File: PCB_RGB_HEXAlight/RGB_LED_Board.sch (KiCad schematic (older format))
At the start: 14 parts, among them P1 CONN_5, U1 RED DRIVER, U2 GREEN DRIVER, U3 BLUEDRIVER

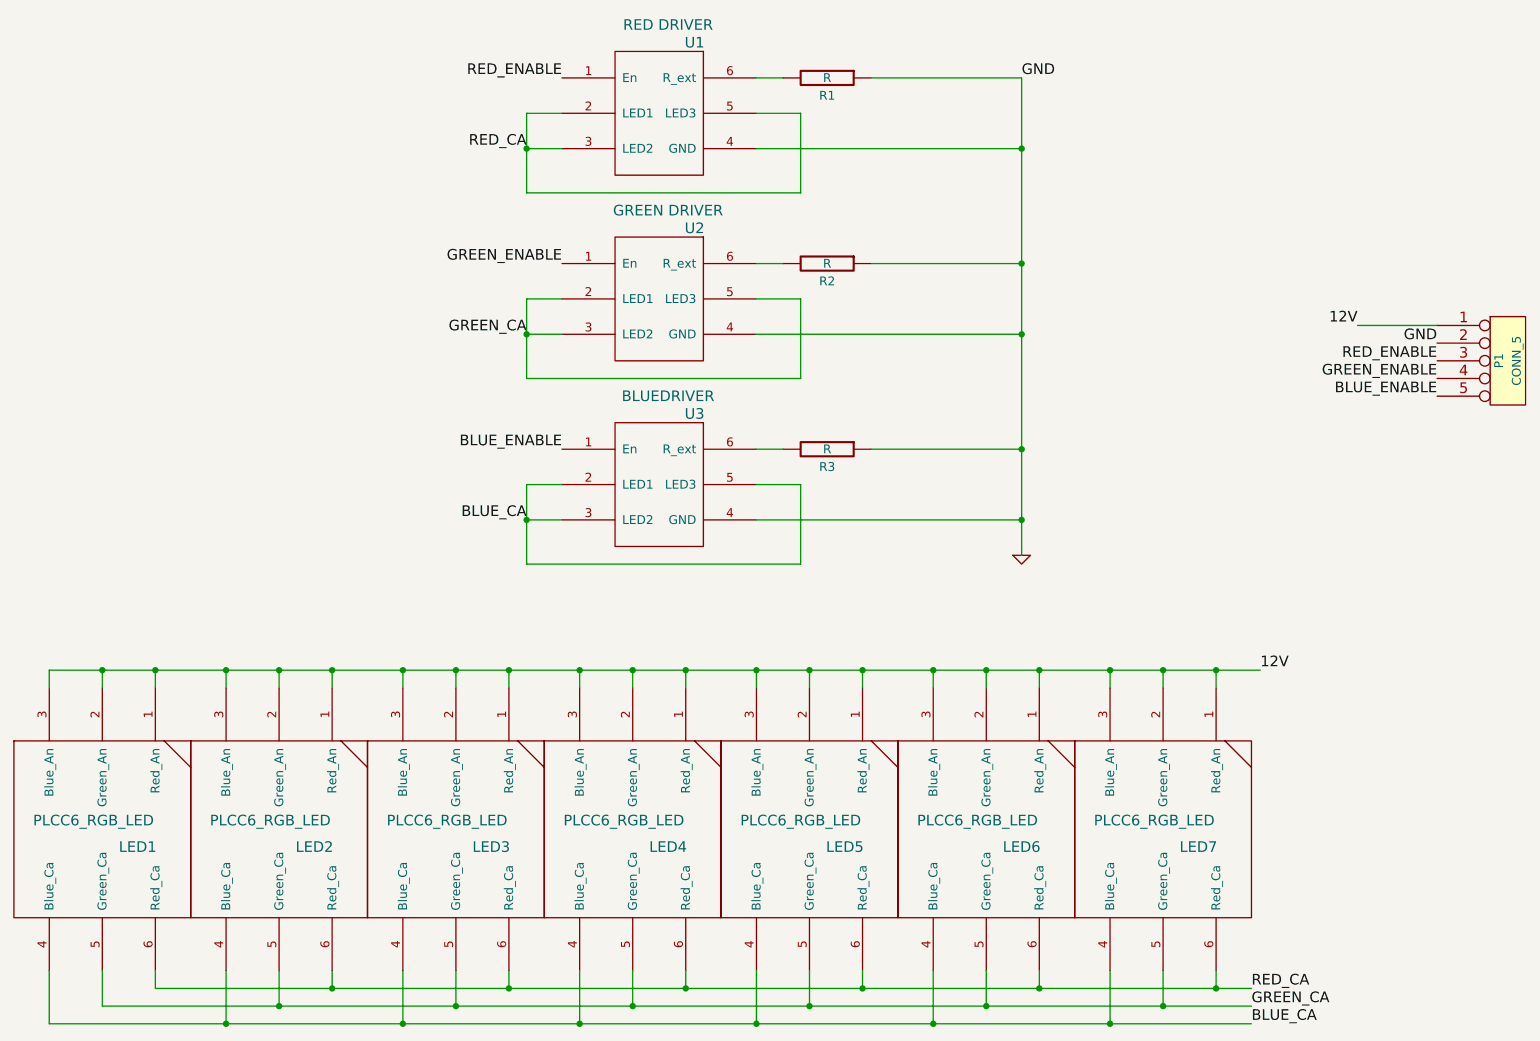
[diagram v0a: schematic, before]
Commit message: Hexagonal Footprint Added
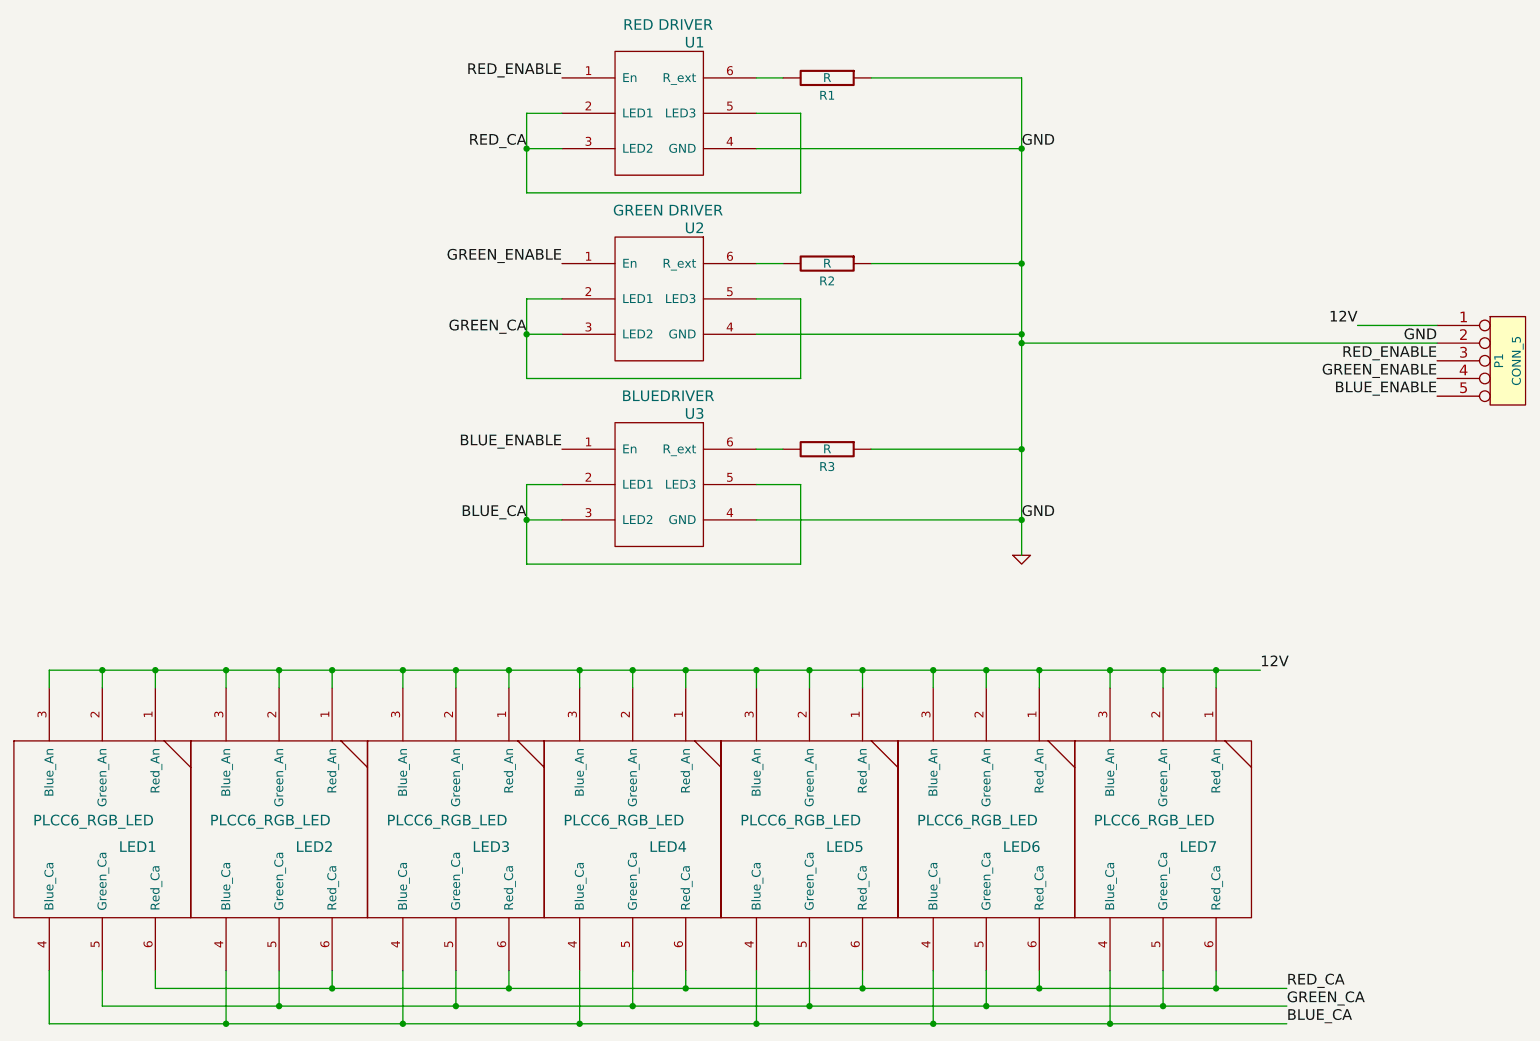
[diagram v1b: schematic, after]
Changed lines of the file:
@@
-EESchema Schematic File Version 2  date Fri 29 Jun 2012 03:46:47 PM EDT
+EESchema Schematic File Version 2  date Fri 06 Jul 2012 05:33:47 PM EDT
 LIBS:power
 LIBS:device
@@
 LIBS:valves
 LIBS:MyLibrary
+LIBS:IHE
 LIBS:RGB_LED_Board-cache
 EELAYER 25  0
@@
 Sheet 1 1
 Title "HEXAlight"
-Date "29 jun 2012"
+Date "6 jul 2012"
 Rev "0"
 Comp "iHeartEngineering"
@@
 Comment4 ""
 $EndDescr
+Connection ~ 7800 2700
+Wire Wire Line
+	10150 2700 7800 2700
+Wire Wire Line
+	9300 6450 2600 6450
 Wire Wire Line
 	7800 3900 7800 1200
@@
 Connection ~ 3600 6450
 Wire Wire Line
-	9100 6450 2600 6450
-Wire Wire Line
 	2600 6450 2600 6250
 Connection ~ 5600 6450
@@
 Wire Wire Line
 	2900 6250 2900 6350
-Wire Wire Line
-	2900 6350 9100 6350
 Connection ~ 3900 6350
 Wire Wire Line
@@
 Wire Wire Line
 	2300 6250 2300 6550
-Wire Wire Line
-	2300 6550 9100 6550
 Connection ~ 3300 6550
 Wire Wire Line
@@
 Wire Wire Line
 	7800 3700 6300 3700
+Wire Wire Line
+	2900 6350 9300 6350
+Wire Wire Line
+	2300 6550 9300 6550
+Text Label 7800 3700 0    60   ~ 0
+GND
+Text Label 7800 1600 0    60   ~ 0
+GND
 $Comp
 L GND #PWR01
@@
 Text Label 5000 2650 2    60   ~ 0
 GREEN_CA
-Text Label 9100 6550 0    60   ~ 0
+Text Label 9300 6550 0    60   ~ 0
 BLUE_CA
-Text Label 9100 6350 0    60   ~ 0
+Text Label 9300 6350 0    60   ~ 0
 RED_CA
-Text Label 9100 6450 0    60   ~ 0
+Text Label 9300 6450 0    60   ~ 0
 GREEN_CA
 Text Label 5000 1600 2    60   ~ 0
@@
 	1    0    0    -1
 $EndComp
-Text Label 7800 1200 0    60   ~ 0
-GND
 Text Label 10150 3000 2    60   ~ 0
 BLUE_ENABLE
